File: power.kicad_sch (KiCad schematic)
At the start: 5 parts

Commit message: Define power flags
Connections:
- net 5V_USB is gone; now on net 5V_Power: C6.1, C8.1, PS2.1 (EN), PS2.6 (VIN)
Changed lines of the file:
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@@
-		)
-	)
-	(label "5V_USB"
-		(at 182.88 80.01 0)
-		(effects
-			(font
-				(size 1.27 1.27)
-			)
-			(justify left bottom)
 		)
 	)
 	(hierarchical_label "12V_Power"
 		(shape output)
-		(at 73.66 77.47 0)
+		(at 203.2 86.36 0)
 		(effects
 			(font
@@
 	(hierarchical_label "5V_Power"
 		(shape input)
-		(at 73.66 73.66 0)
+		(at 182.88 80.01 0)
 		(effects
 			(font

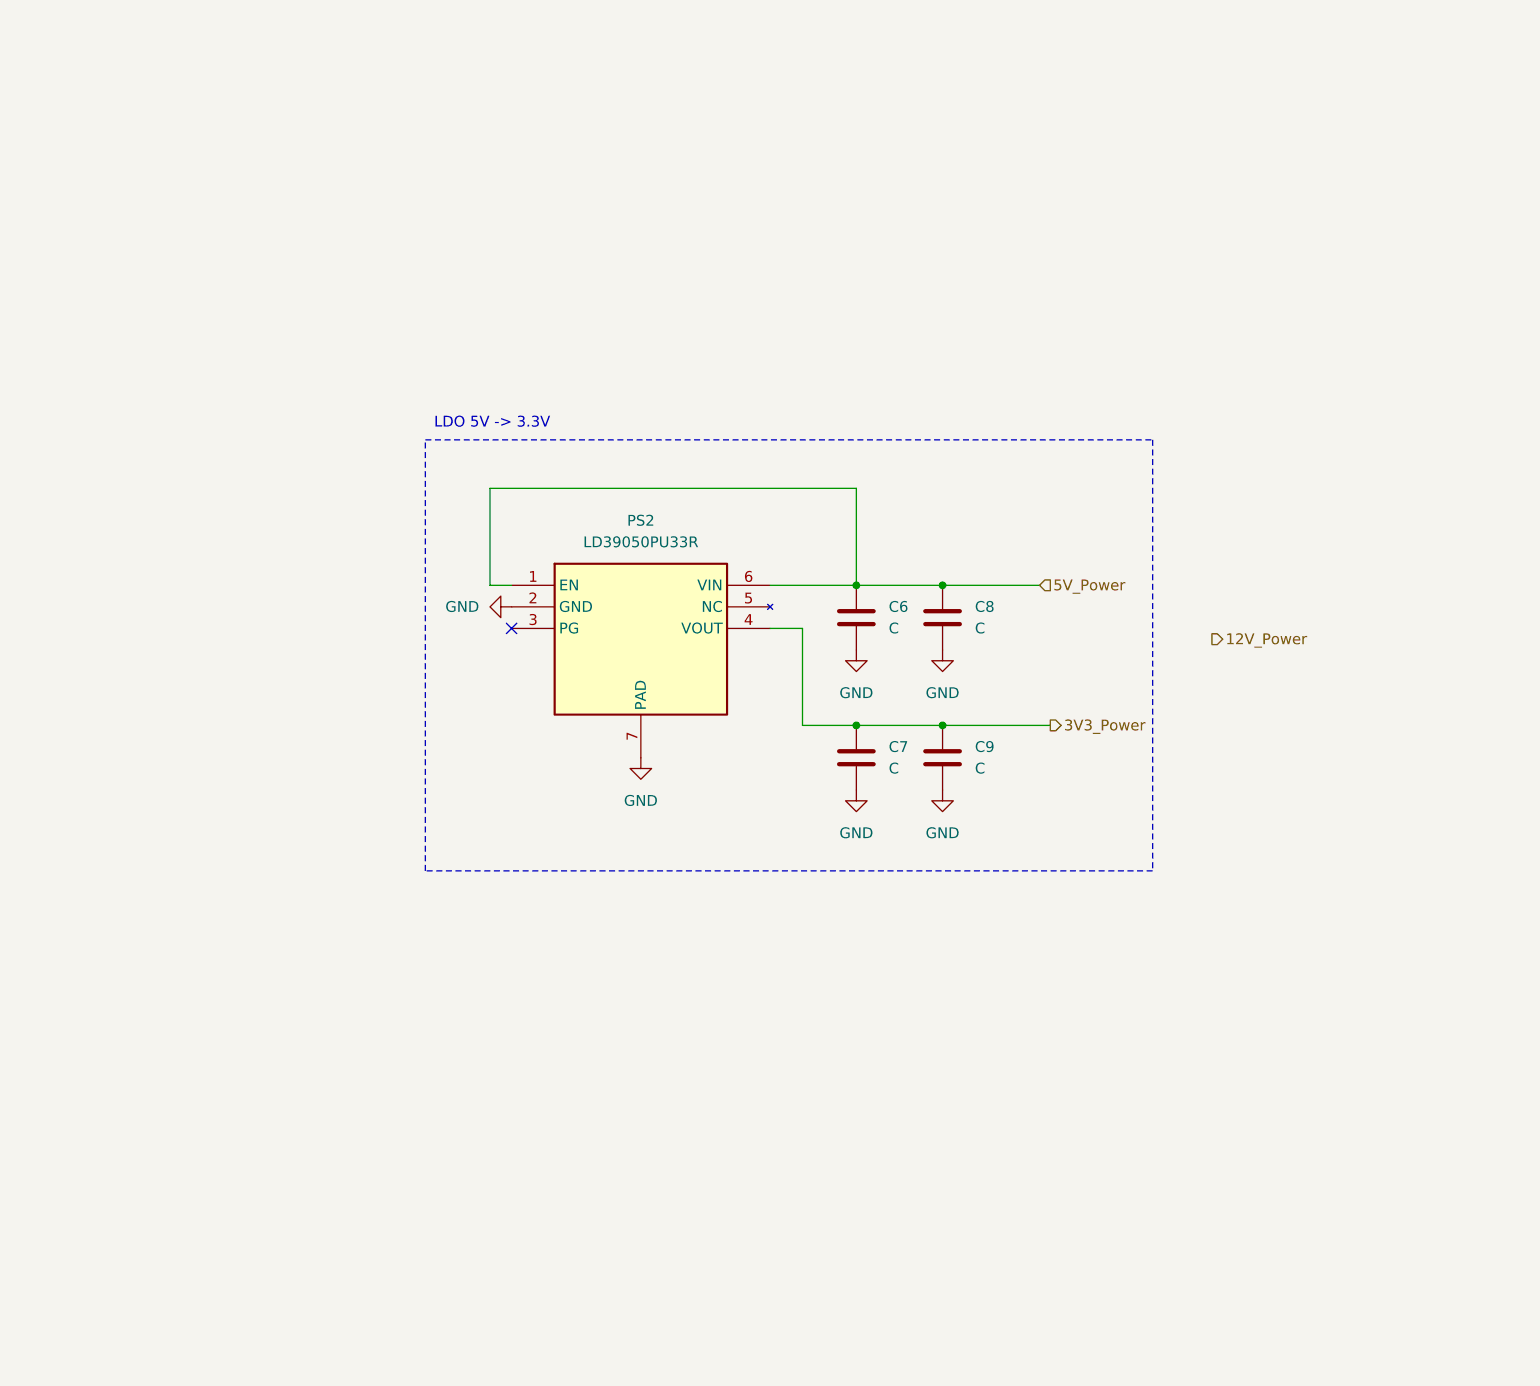
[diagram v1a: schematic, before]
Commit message: Add WLED driver in power shcematic
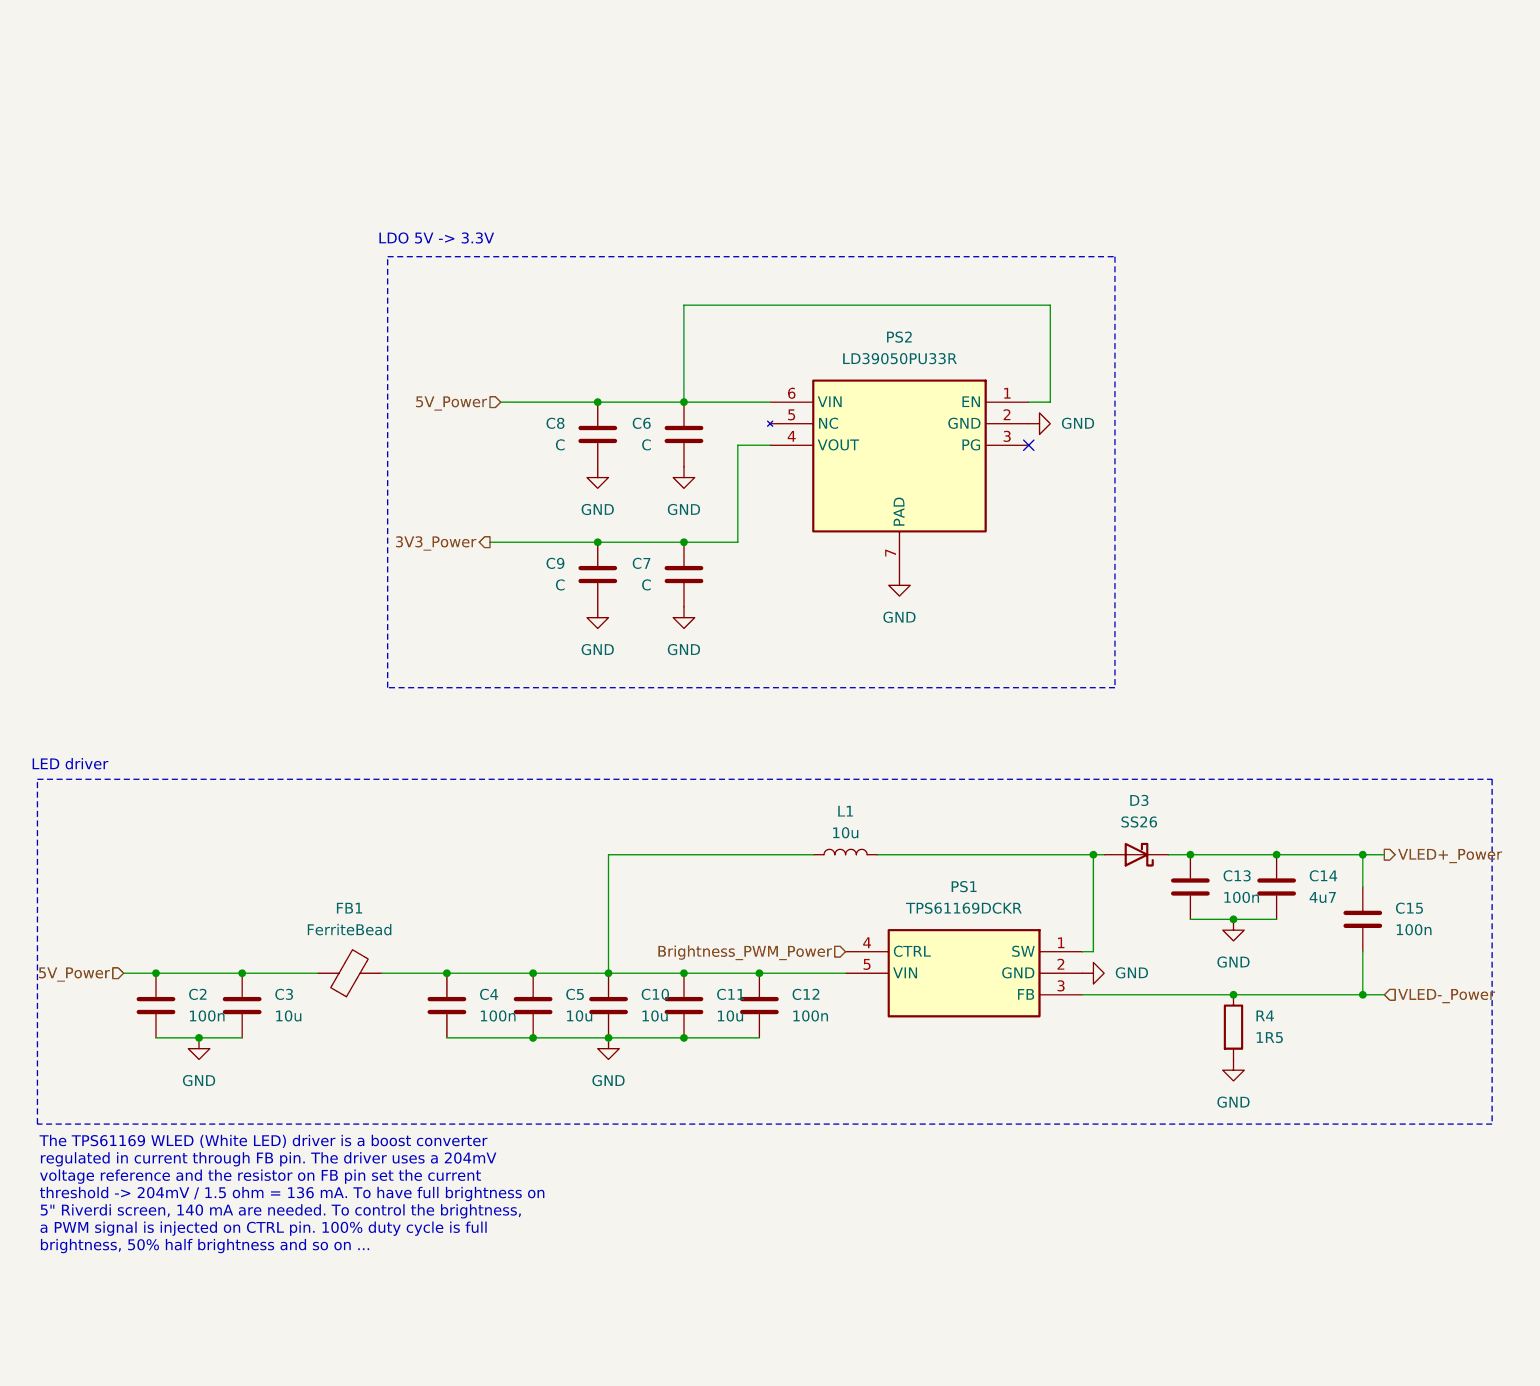
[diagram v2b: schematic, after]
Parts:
- added C10, C11, C3, C5: 10u, symbol Device:C
- added C12, C13, C15, C2, C4: 100n, symbol Device:C
- added C14: 4u7, symbol Device:C
- added D3: SS26, Diode_SMD:D_SMA, symbol Diode:SS26
- added FB1: FerriteBead, Inductor_SMD:L_0603_1608Metric_Pad1.05x0.95mm_HandSolder, symbol Device:FerriteBead
- added L1: 10u, symbol Device:L
- added PS1: TPS61169DCKR, SOT65P210X110-5N, symbol weather-station-poc-sym:TPS61169DCKR
- added R4: 1R5, symbol Device:R
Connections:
- net 5V_Power: now also C2.1, C3.1, FB1.1
- net GND: now also C10.2, C11.2, C12.2, C13.2, C14.2, C2.2, C3.2, C4.2, C5.2, PS1.2 (GND), R4.2
- new net: D3.2 (A), L1.2, PS1.1 (SW)
- new net: C10.1, C11.1, C12.1, C4.1, C5.1, FB1.2, L1.1, PS1.5 (VIN)
- new net Brightness_PWM_Power: PS1.4 (CTRL)
- new net VLED+_Power: C13.1, C14.1, C15.1, D3.1 (K)
- new net VLED-_Power: C15.2, PS1.3 (FB), R4.1
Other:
- note added: "LED driver"
- note added: "The TPS61169 WLED (White LED) driver is a boost converter regulated in current through FB pin. The driver uses a 204mV voltage reference and the resistor on FB pin set the current threshold -> 204mV / 1.5 ohm = 136 mA. To have full brightness on 5" Riverdi screen, 140 mA are needed. To control the brightness, a PWM signal is injected on CTRL pin. 100% duty cycle is full brightness, 50% half brigh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"
- moved on the sheet: C6, C7, C8, C9, PS2

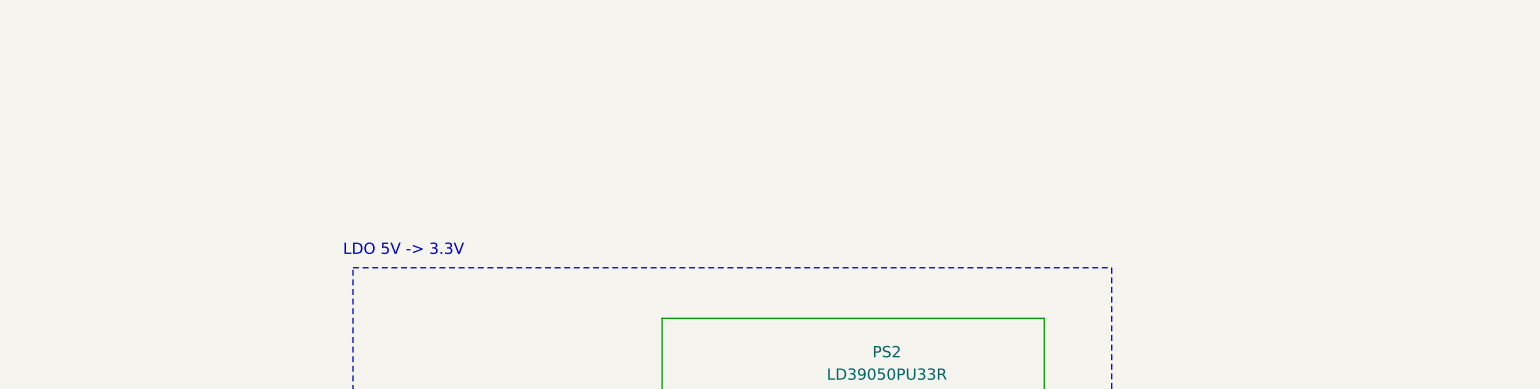
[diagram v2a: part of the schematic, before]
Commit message: Use local labels for RGB bus in folio and add title for all folio
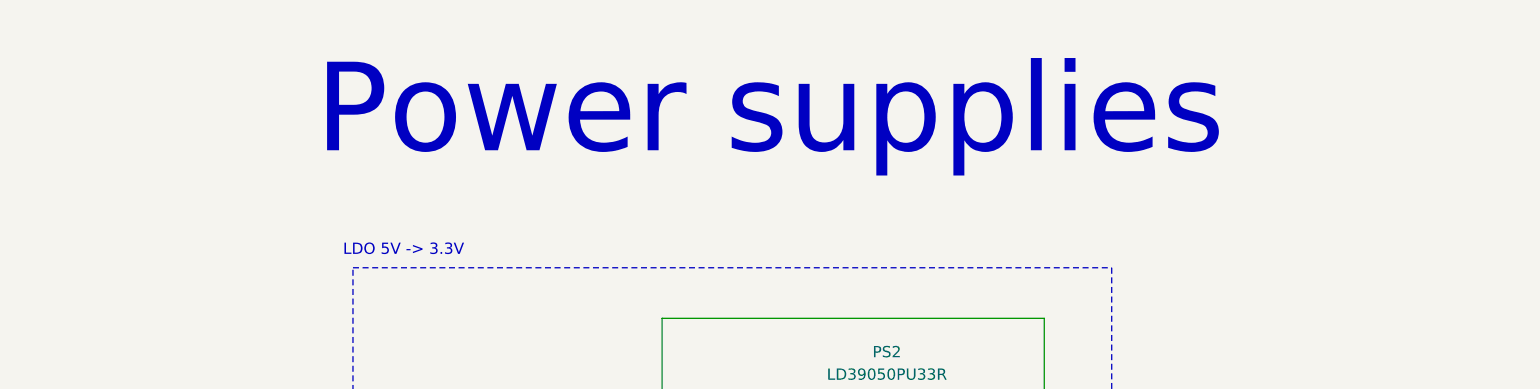
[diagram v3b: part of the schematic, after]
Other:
- note added: "Power supplies"
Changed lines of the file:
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@@
+		)
+	)
+	(text "Power supplies"
+		(exclude_from_sim no)
+		(at 153.162 23.622 0)
+		(effects
+			(font
+				(size 10 10)
+			)
 		)
 	)

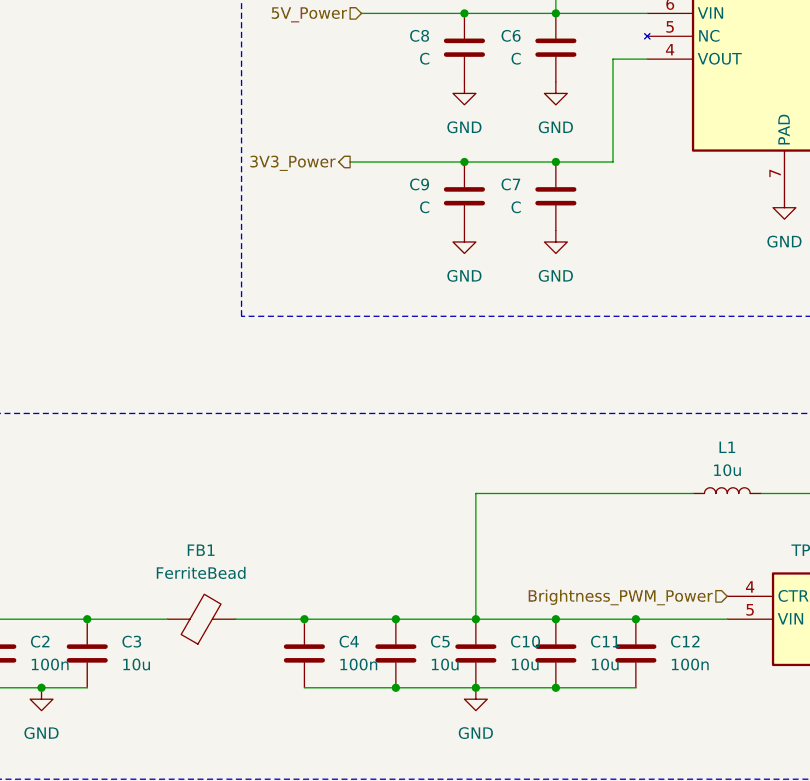
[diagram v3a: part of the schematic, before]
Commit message: Fix some ERC errors
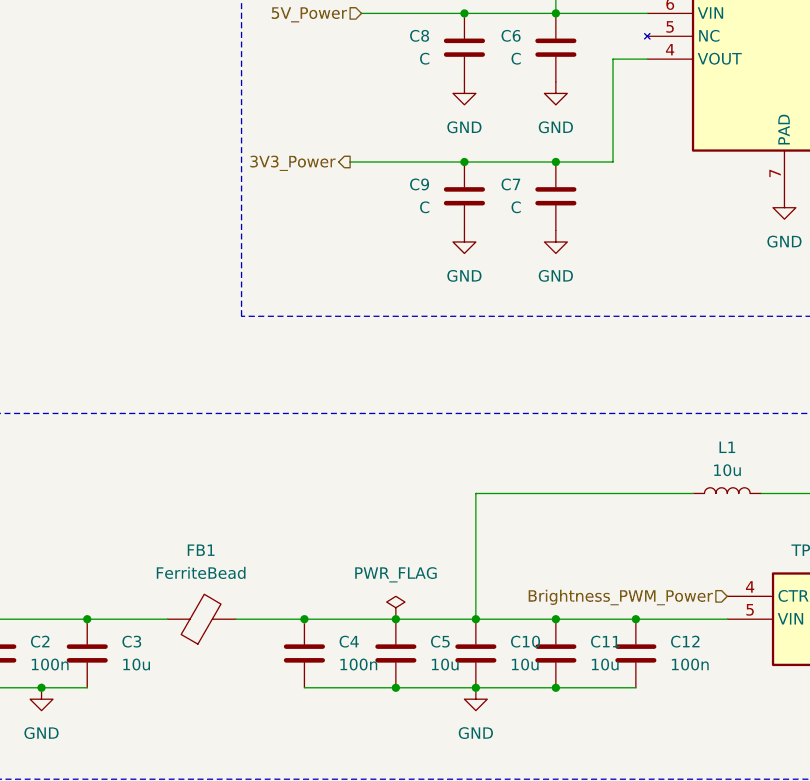
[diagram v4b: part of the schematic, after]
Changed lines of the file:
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@@
-	(wire
-		(pts
-			(xy 130.81 74.93) (xy 118.11 74.93)
-		)
-		(stroke
-			(width 0)
-			(type default)
-		)
-	)
 	(wire
 		(pts
@@
 		(pts
 			(xy 220.98 111.76) (xy 220.98 115.57)
+		)
+		(stroke
+			(width 0)
+			(type default)
+		)
+	)
+	(wire
+		(pts
+			(xy 118.11 74.93) (xy 130.81 74.93)
 		)
 		(stroke
@@
 					(unit 1)
 				)
+			)
+		)
+	)
+	(symbol
+		(lib_id "power:PWR_FLAG")
+		(at 123.19 125.73 0)
+		(unit 1)
+		(exclude_from_sim no)
+		(in_bom yes)
+		(on_board yes)
+		(dnp no)
+		(fields_autoplaced yes)
+		(property "Reference" "#FLG05"
+			(at 123.19 123.825 0)
+			(effects
+				(font
+					(size 1.27 1.27)
+				)
+				(hide yes)
+			)
+		)
+		(property "Value" "PWR_FLAG"
+			(at 123.19 120.65 0)
+			(effects
+				(font
+					(size 1.27 1.27)
+				)
+			)
+		)
+		(property "Footprint" ""
+			(at 123.19 125.73 0)
+			(effects
+				(font
+					(size 1.27 1.27)
+				)
+				(hide yes)
+			)
+		)
+		(property "Datasheet" "~"
+			(at 123.19 125.73 0)
+			(effects
+				(font
+					(size 1.27 1.27)
+				)
+				(hide yes)
+			)
+		)
+		(property "Description" "Special symbol for telling ERC where power comes from"
+			(at 123.19 125.73 0)
+			(effects
+				(font
+					(size 1.27 1.27)
+				)
+				(hide yes)
+			)
+		)
+		(pin "1"
+		)
+		(instances
+			(project ""
+				(path "/38eb53bb-294e-46e4-ad59-fd355ca373b9/12325ae0-3782-4eae-9f35-258d08cb4f7e"
+					(reference "#FLG05")
+					(unit 1)
+				)

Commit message: Fix warnings for footprint
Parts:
- PS1: footprint SOT65P210X110-5N -> weather-station-poc-fp:SOT65P210X110-5N
- PS2: footprint SON95P300X300X100-7N-D -> weather-station-poc-fp:SON95P300X300X100-7N-D
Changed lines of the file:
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@@
 			)
 		)
-		(property "Footprint" "SON95P300X300X100-7N-D"
+		(property "Footprint" "weather-station-poc-fp:SON95P300X300X100-7N-D"
 			(at 154.94 153.34 0)
 			(effects
@@
 			)
 		)
-		(property "Footprint" "SOT65P210X110-5N"
+		(property "Footprint" "weather-station-poc-fp:SOT65P210X110-5N"
 			(at 163.83 218.11 0)
 			(effects

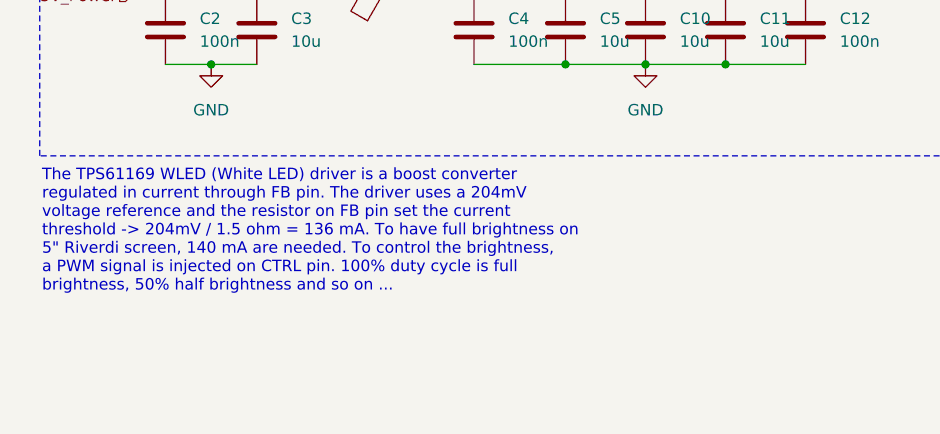
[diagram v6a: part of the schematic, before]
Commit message: Functionnal block delimiting in schematics
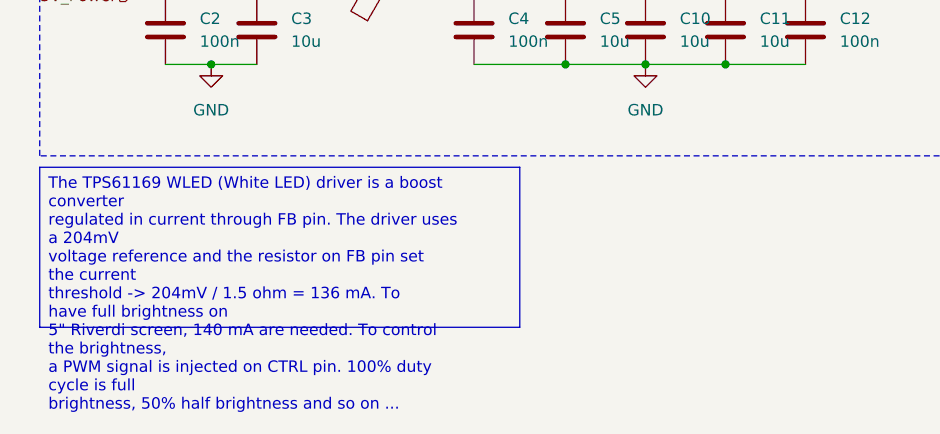
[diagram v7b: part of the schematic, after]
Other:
- note removed: "The TPS61169 WLED (White LED) driver is a boost converter regulated in current through FB pin. The driver uses a 204mV voltage reference and the resistor on FB pin set the current threshold -> 204mV / 1.5 ohm = 136 mA. To have full brightness on 5" Riverdi screen, 140 mA are needed. To control the brightness, a PWM signal is injected on CTRL pin. 100% duty cycle is full brightness, 50% half brigh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"
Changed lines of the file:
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@@
 		)
 	)
-	(text "The TPS61169 WLED (White LED) driver is a boost converter\nregulated in current through FB pin. The driver uses a 204mV\nvoltage reference and the resistor on FB pin set the current\nthreshold -> 204mV / 1.5 ohm = 136 mA. To have full brightness on\n5\" Riverdi screen, 140 mA are needed. To control the brightness,\na PWM signal is injected on CTRL pin. 100% duty cycle is full\nbrightness, 50% half brightness and so on ... "
+	(text_box "The TPS61169 WLED (White LED) driver is a boost converter\nregulated in current through FB pin. The driver uses a 204mV\nvoltage reference and the resistor on FB pin set the current\nthreshold -> 204mV / 1.5 ohm = 136 mA. To have full brightness on\n5\" Riverdi screen, 140 mA are needed. To control the brightness,\na PWM signal is injected on CTRL pin. 100% duty cycle is full\nbrightness, 50% half brightness and so on ... "
 		(exclude_from_sim no)
-		(at 65.024 151.892 0)
+		(at 64.77 144.78 0)
+		(size 53.34 17.78)
+		(margins 0.9525 0.9525 0.9525 0.9525)
+		(stroke
+			(width 0)
+			(type solid)
+		)
+		(fill
+			(type none)
+		)
 		(effects
 			(font
 				(size 1.27 1.27)
 			)
-			(justify left)
+			(justify left top)
 		)
 	)
